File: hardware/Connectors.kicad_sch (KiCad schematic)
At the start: 4 parts, among them J3 FTSH-107-01-L-D-K, J4 Conn_02x02_Counter_Clockwise

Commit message: reorganization of project folders acording to templates
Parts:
- J3: footprint SamacSys_Parts:FTSH-107-XX-YYY-D-K -> Samacsys:FTSH-107-XX-YYY-D-K
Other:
- moved on the sheet: J3

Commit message: reorganize SPI signals into bus
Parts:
- J3: footprint Samacsys:FTSH-107-XX-YYY-D-K -> XiaoS3:SAMTEC_FTSH-107-01-L-D-K
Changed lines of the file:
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@@
 			)
 		)
-		(property "Footprint" "Samacsys:FTSH-107-XX-YYY-D-K"
+		(property "Footprint" "XiaoS3:SAMTEC_FTSH-107-01-L-D-K"
 			(at 179.07 196.52 0)
 			(hide yes)

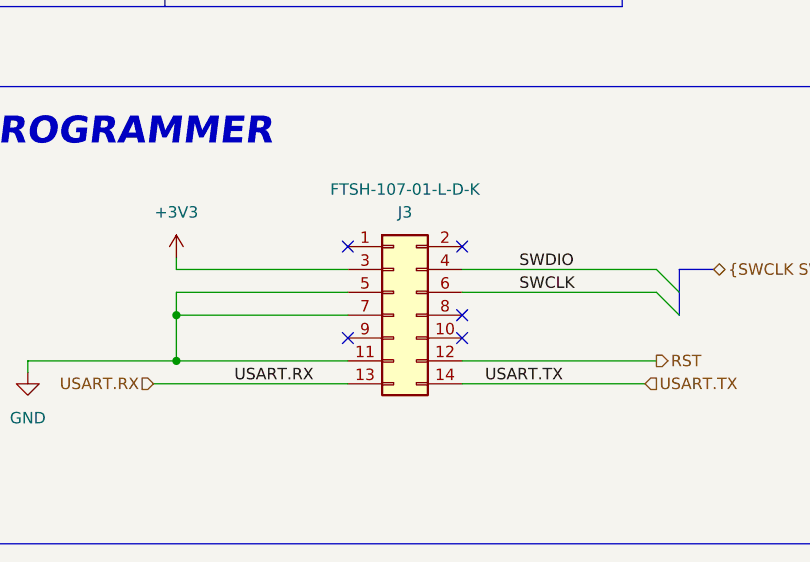
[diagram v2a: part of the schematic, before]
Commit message: initial component placement
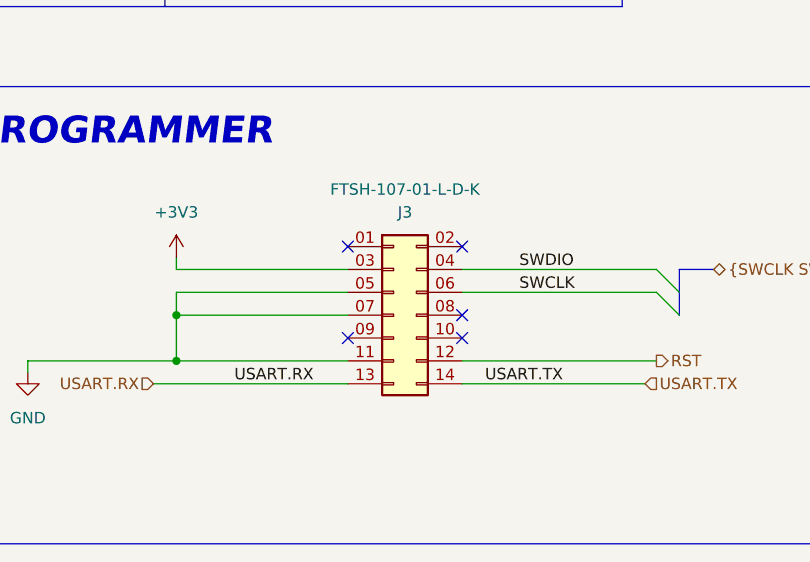
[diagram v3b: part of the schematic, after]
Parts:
- J4: footprint (none) -> Connector_JST:JST_EH_S4B-EH_1x04_P2.50mm_Horizontal
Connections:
- net +3V3: now also J3.03 (Pin_3); no longer J3.3 (Pin_3)
- net GND: now also J3.05 (Pin_5), J3.07 (Pin_7); no longer J3.5 (Pin_5), J3.7 (Pin_7)
- net SWCLK: now also J3.06 (Pin_6); no longer J3.6 (Pin_6)
- net SWDIO: now also J3.04 (Pin_4); no longer J3.4 (Pin_4)
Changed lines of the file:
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@@
 			)
 		)
-		(property "Footprint" ""
+		(property "Footprint" "Connector_JST:JST_EH_S4B-EH_1x04_P2.50mm_Horizontal"
 			(at 152.4 50.8 0)
 			(hide yes)
@@
 			)
 		)
-		(pin "2"
-		)
-		(pin "5"
-		)
-		(pin "8"
+		(pin "08"
+		)
+		(pin "07"
+		)
+		(pin "05"
 		)
 		(pin "11"
 		)
-		(pin "4"
-		)
-		(pin "7"
+		(pin "06"
+		)
+		(pin "09"
 		)
 		(pin "10"
@@
 		(pin "12"
 		)
-		(pin "6"
+		(pin "03"
 		)
 		(pin "13"
 		)
-		(pin "3"
+		(pin "02"
 		)
 		(pin "14"
 		)
-		(pin "9"
-		)
-		(pin "1"
+		(pin "04"
+		)
+		(pin "01"
 		)
 		(instances

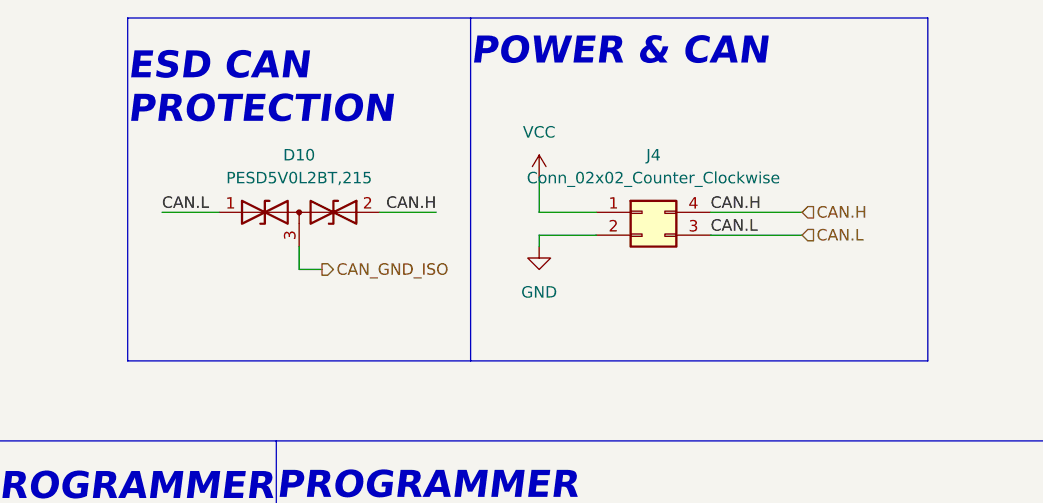
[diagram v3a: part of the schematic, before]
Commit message: changed layout
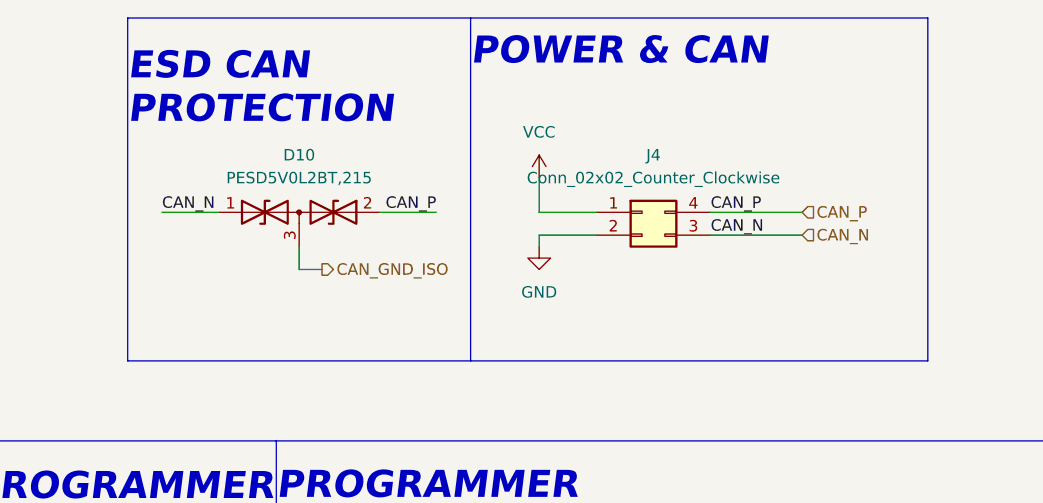
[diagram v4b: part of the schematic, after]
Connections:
- net CAN.H renamed CAN_P
- net CAN.L renamed CAN_N
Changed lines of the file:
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@@
 		)
 	)
-	(label "CAN.H"
+	(label "CAN_P"
 		(at 160.02 50.8 0)
 		(effects
@@
 		)
 	)
-	(label "CAN.L"
+	(label "CAN_N"
 		(at 99.06 50.8 0)
 		(effects
@@
 		)
 	)
-	(label "CAN.L"
+	(label "CAN_N"
 		(at 160.02 53.34 0)
 		(effects
@@
 		)
 	)
-	(label "CAN.H"
+	(label "CAN_P"
 		(at 129.54 50.8 180)
 		(effects
@@
 		)
 	)
-	(hierarchical_label "CAN.H"
+	(hierarchical_label "CAN_P"
 		(shape input)
 		(at 170.18 50.8 0)
@@
 		)
 	)
-	(hierarchical_label "CAN.L"
+	(hierarchical_label "CAN_N"
 		(shape input)
 		(at 170.18 53.34 0)

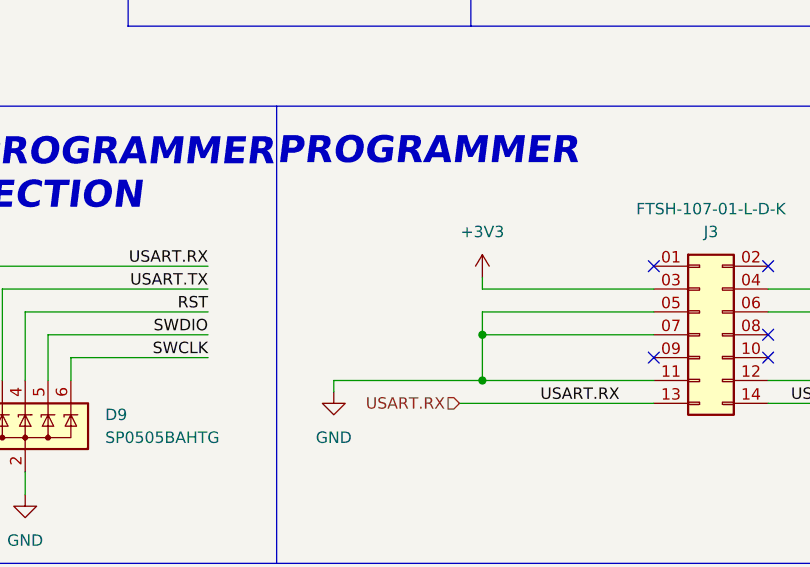
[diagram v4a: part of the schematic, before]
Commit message: added missing TVS diode
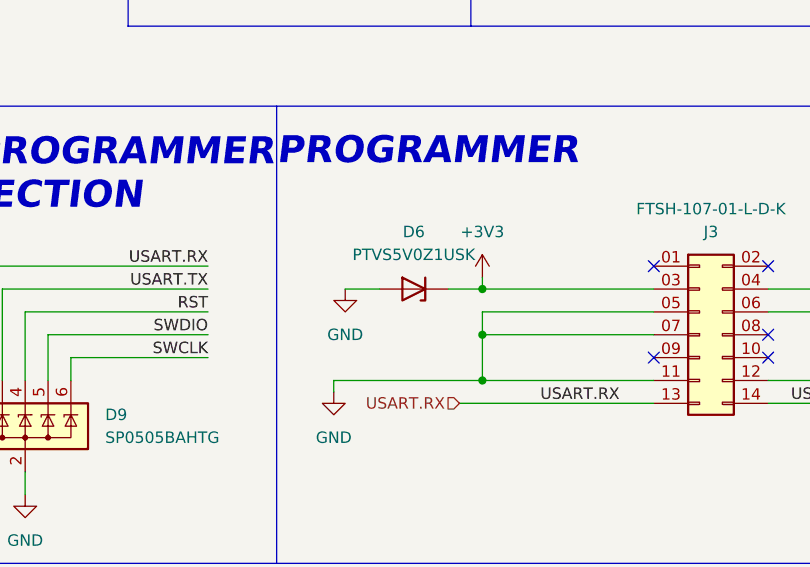
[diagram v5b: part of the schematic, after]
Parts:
- added D6: PTVS5V0Z1USK, Diode_SMD:D_SOD-323_HandSoldering, symbol Diode:PTVS5V0Z1USK
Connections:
- net +3V3: now also D6.1 (K)
- net GND: now also D6.2 (A)
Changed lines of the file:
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@@
+	)
+	(junction
+		(at 134.62 96.52)
+		(diameter 0)
+		(color 0 0 0 0)
 	)
 	(junction
@@
 	(wire
 		(pts
+			(xy 119.38 96.52) (xy 123.19 96.52)
+		)
+		(stroke
+			(width 0)
+			(type default)
+		)
+	)
+	(wire
+		(pts
 			(xy 78.74 106.68) (xy 78.74 93.98)
 		)
@@
 		(pts
 			(xy 81.28 96.52) (xy 104.14 96.52)
+		)
+		(stroke
+			(width 0)
+			(type default)
+		)
+	)
+	(wire
+		(pts
+			(xy 130.81 96.52) (xy 134.62 96.52)
 		)
 		(stroke
@@
 	(symbol
 		(lib_id "power:GND")
+		(at 119.38 96.52 0)
+		(unit 1)
+		(body_style 1)
+		(exclude_from_sim no)
+		(in_bom yes)
+		(on_board yes)
+		(in_pos_files yes)
+		(dnp no)
+		(fields_autoplaced yes)
+		(property "Reference" "#PWR029"
+			(at 119.38 102.87 0)
+			(hide yes)
+			(show_name no)
+			(do_not_autoplace no)
+			(effects
+				(font
+					(size 1.27 1.27)
+				)
+			)
+		)
+		(property "Value" "GND"
+			(at 119.38 101.6 0)
+			(show_name no)
+			(do_not_autoplace no)
+			(effects
+				(font
+					(size 1.27 1.27)
+				)
+			)
+		)
+		(property "Footprint" ""
+			(at 119.38 96.52 0)
+			(hide yes)
+			(show_name no)
+			(do_not_autoplace no)
+			(effects
+				(font
+					(size 1.27 1.27)
+				)
+			)
+		)
+		(property "Datasheet" ""
+			(at 119.38 96.52 0)
+			(hide yes)
+			(show_name no)
+			(do_not_autoplace no)
+			(effects
+				(font
+					(size 1.27 1.27)
+				)
+			)
+		)
+		(property "Description" "Power symbol creates a global label with name \"GND\" , ground"
+			(at 119.38 96.52 0)
+			(hide yes)
+			(show_name no)
+			(do_not_autoplace no)
+			(effects
+				(font
+					(size 1.27 1.27)
+				)
+			)
+		)
+		(pin "1"
+		)
+		(instances
+			(project "tire_pressure_interface"
+				(path "/b652b05a-4e3d-4ad1-b032-18886abe7d45/24d2ddf3-2016-4f01-82b4-08db856ba16e"
+					(reference "#PWR029")
+					(unit 1)
+				)
+			)
+		)
+	)
+	(symbol
+		(lib_id "power:GND")
 		(at 118.11 107.95 0)
 		(unit 1)
@@
 					(unit 1)
 				)
+			)
+		)
+	)
+	(symbol
+		(lib_id "Diode:PTVS5V0Z1USK")
+		(at 127 96.52 180)
+		(unit 1)
+		(body_style 1)
+		(exclude_from_sim no)
+		(in_bom yes)
+		(on_board yes)
+		(in_pos_files yes)
+		(dnp no)
+		(fields_autoplaced yes)
+		(property "Reference" "D6"
+			(at 127 90.17 0)
+			(show_name no)
+			(do_not_autoplace no)
+			(effects
+				(font
+					(size 1.27 1.27)
+				)
+			)
+		)
+		(property "Value" "PTVS5V0Z1USK"
+			(at 127 92.71 0)
+			(show_name no)
+			(do_not_autoplace no)
+			(effects
+				(font
+					(size 1.27 1.27)
+				)
+			)
+		)
+		(property "Footprint" "Diode_SMD:D_SOD-323_HandSoldering"
+			(at 127 92.075 0)
+			(hide yes)
+			(show_name no)
+			(do_not_autoplace no)
+			(effects
+				(font
+					(size 1.27 1.27)
+				)
+			)
+		)
+		(property "Datasheet" "https://semtech.my.salesforce.com/sfc/p/E0000000JelG/a/44000000MCod/Fs.eSBQs1U.304Nkc5rxRZ3Lk6_1A4.ZX_npjU1R.C8"
+			(at 127 96.52 0)
+			(hide yes)
+			(show_name no)
+			(do_not_autoplace no)
+			(effects
+				(font
+					(size 1.27 1.27)
+				)
+			)
+		)
+		(property "Description" "ESD Protection Diodes / TVS Diodes TVS 1-LINE UNI,10A(8/20)5.3V"
+			(at 127 96.52 0)
+			(hide yes)
+			(show_name no)
+			(do_not_autoplace no)
+			(effects
+				(font
+					(size 1.27 1.27)
+				)
+			)
+		)
+		(property "Mouser number" "947-UCLAMP3301D.TCT"
+			(at 127 96.52 0)
+			(hide yes)
+			(show_name no)
+			(do_not_autoplace no)
+			(effects
+				(font
+					(size 1.27 1.27)
+				)
+			)
+		)
+		(property "Mouser price/stock" "https://www.mouser.pl/ProductDetail/Semtech/UCLAMP3301D.TCT?qs=rBWM4%252BvDhIcs1MIPFV0RMQ%3D%3D"
+			(at 127 96.52 0)
+			(hide yes)
+			(show_name no)
+			(do_not_autoplace no)
+			(effects
+				(font
+					(size 1.27 1.27)
+				)
+			)
+		)
+		(pin "2"
+		)
+		(pin "1"
+		)
+		(instances
+			(project "tire_pressure_interface"
+				(path "/b652b05a-4e3d-4ad1-b032-18886abe7d45/24d2ddf3-2016-4f01-82b4-08db856ba16e"
+					(reference "D6")
+					(unit 1)
+				)

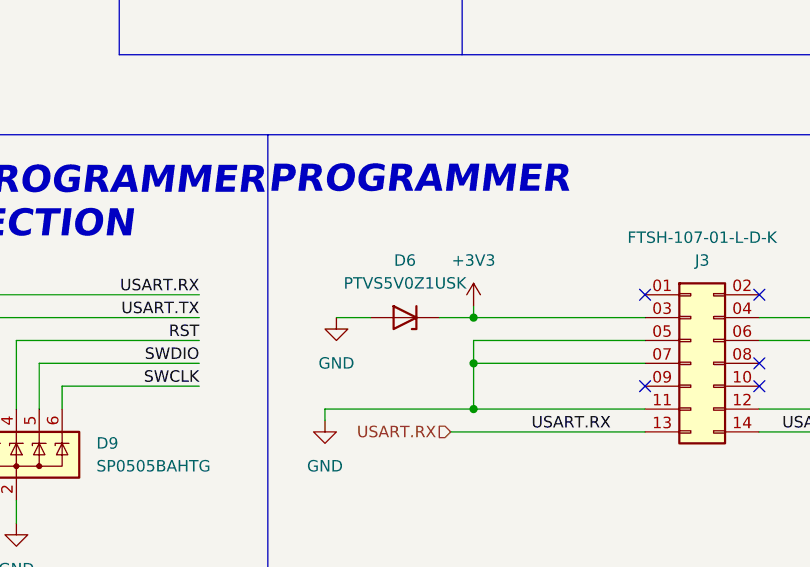
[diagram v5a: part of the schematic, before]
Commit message: added missing TVS diode
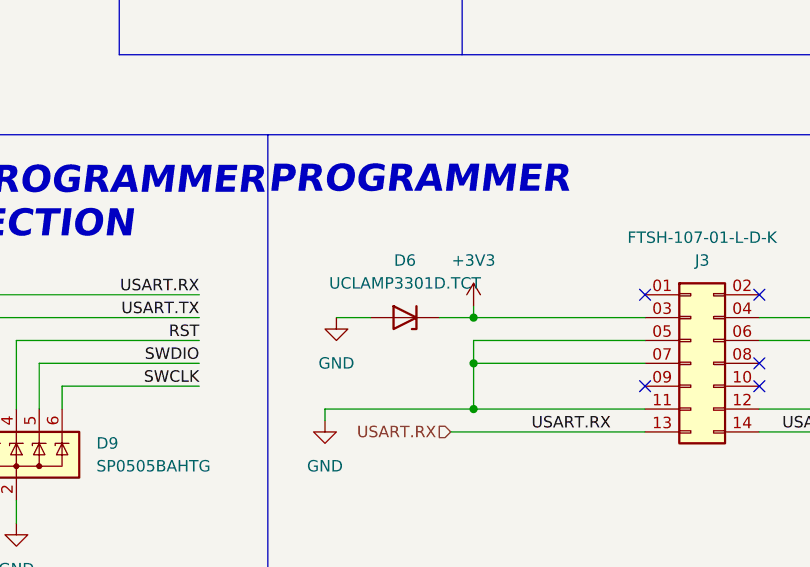
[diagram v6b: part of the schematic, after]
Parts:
- D6: value PTVS5V0Z1USK -> UCLAMP3301D.TCT
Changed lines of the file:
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@@
 			)
 		)
-		(property "Value" "PTVS5V0Z1USK"
+		(property "Value" "UCLAMP3301D.TCT"
 			(at 127 92.71 0)
 			(show_name no)
